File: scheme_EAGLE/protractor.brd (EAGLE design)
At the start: 160 x 100 mm, 20 parts, among them T1 BT136, U1 ATTINY45-20PU

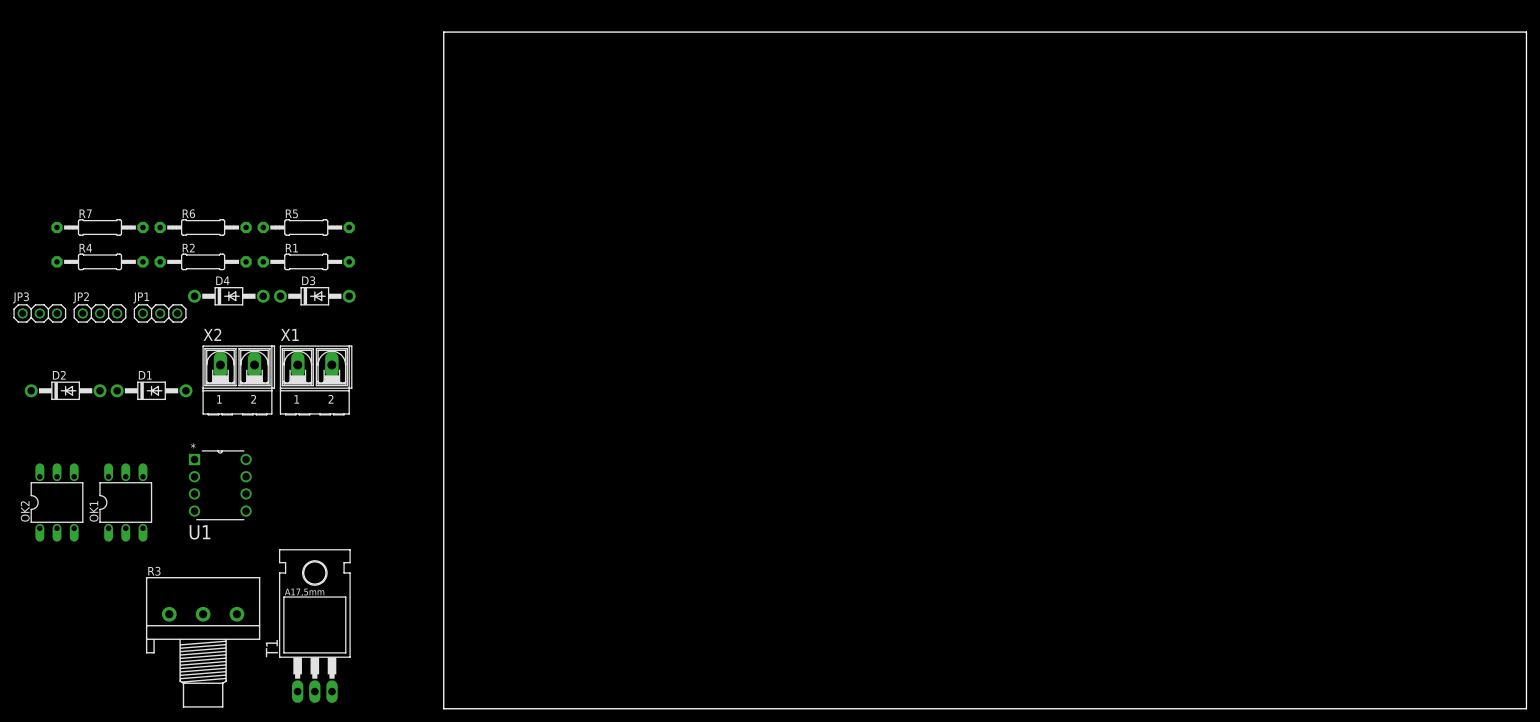
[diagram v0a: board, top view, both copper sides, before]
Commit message: Make the first version of the dimmer board
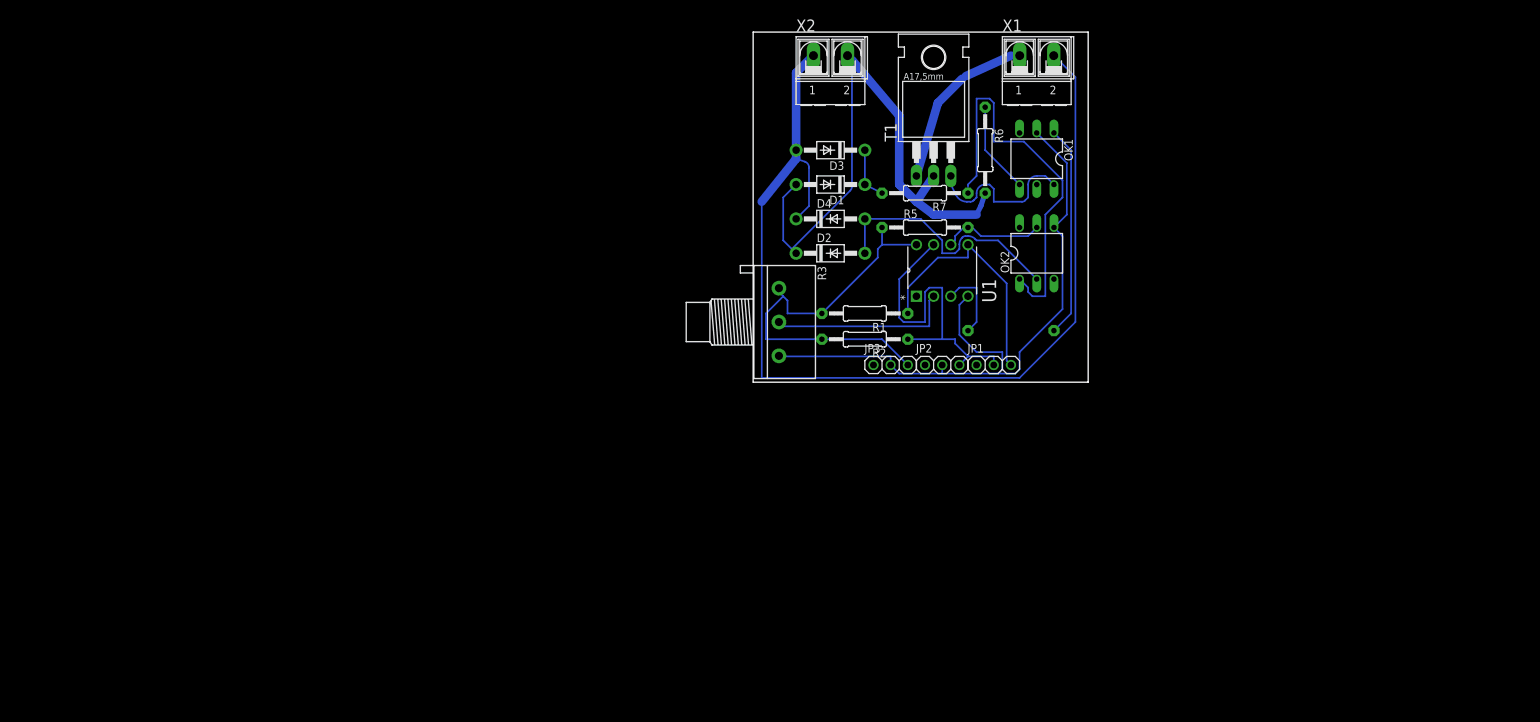
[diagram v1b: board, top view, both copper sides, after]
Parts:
- moved OK2 149.4 mm to (87.6, 67.3)
- moved OK1 143.9 mm to (87.6, 81.3), turned to 180 degrees
- moved R4 135.0 mm to (83.8, 55.9), flipped to the bottom, turned to 180 degrees
- moved JP3 126.0 mm to (66.0, 50.8)
- moved JP2 124.7 mm to (73.7, 50.8)
- moved JP1 123.4 mm to (81.3, 50.8)
- moved R7 122.0 mm to (71.1, 76.2), turned to 180 degrees
- moved T1 119.0 mm to (72.4, 85.1)
- moved R6 116.1 mm to (80.0, 82.5), turned to 270 degrees
- moved X1 116.1 mm to (87.6, 96.5)
- moved D2 114.8 mm to (57.1, 67.3)
- moved U1 113.7 mm to (77.5, 68.6), turned to 90 degrees
- moved D1 104.9 mm to (57.1, 77.5), turned to 180 degrees
- moved X2 98.8 mm to (57.1, 96.5)
- moved R2 98.5 mm to (62.2, 54.6), turned to 180 degrees
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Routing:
- net N$3: track 0.00 -> 151.8 mm
- net GND: track 0.00 -> 96.8 mm
- net N$4: track 0.00 -> 87.2 mm
- net VCC: track 0.00 -> 60.7 mm
- net N$5: track 0.00 -> 59.0 mm
- net N$14: track 0.00 -> 49.0 mm
- net N$1: track 0.00 -> 37.9 mm
- net N$11: track 0.00 -> 36.9 mm
- net N$13: track 0.00 -> 31.3 mm
- net N$9: track 0.00 -> 27.6 mm
- net N$8: track 0.00 -> 25.6 mm
- net N$6: track 0.00 -> 24.5 mm
- net N$10: track 0.00 -> 15.2 mm
- net N$7: track 0.00 -> 13.5 mm
- net N$12: track 0.00 -> 11.2 mm
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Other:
- board size 160 x 100 mm -> 49.5 x 51.7 mm

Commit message: Route configured.
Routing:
- net N$9: track 27.6 -> 58.7 mm
- net N$3: track 151.8 -> 179.0 mm
- net N$5: track 59.0 -> 37.4 mm
- net GND: track 96.8 -> 115.5 mm
- net N$14: track 49.0 -> 33.6 mm
- net N$1: track 37.9 -> 46.3 mm
- net N$6: track 24.5 -> 31.4 mm
- net N$4: track 87.2 -> 82.0 mm
- net N$12: track 11.2 -> 6.13 mm
- net N$8: track 25.6 -> 29.8 mm
- net N$11: track 36.9 -> 33.8 mm
- net N$13: track 31.3 -> 33.4 mm
- net VCC: track 60.7 -> 59.7 mm
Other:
- board size 49.5 x 51.7 mm -> 53.3 x 56.2 mm

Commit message: Now, the firmware is works
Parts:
- .: value ATTINY45-20PU -> attiny
- renumbered U1 to .
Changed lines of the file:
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@@
 <?xml version="1.0" encoding="utf-8"?>
 <!DOCTYPE eagle SYSTEM "eagle.dtd">
-<eagle version="7.2.0">
+<eagle version="7.5.0">
 <drawing>
 <settings>
@@
 <layer number="15" name="Route15" color="4" fill="6" visible="no" active="no"/>
 <layer number="16" name="Bottom" color="1" fill="1" visible="yes" active="yes"/>
-<layer number="17" name="Pads" color="2" fill="1" visible="yes" active="yes"/>
-<layer number="18" name="Vias" color="2" fill="1" visible="yes" active="yes"/>
-<layer number="19" name="Unrouted" color="6" fill="1" visible="yes" active="yes"/>
+<layer number="17" name="Pads" color="2" fill="1" visible="no" active="yes"/>
+<layer number="18" name="Vias" color="2" fill="1" visible="no" active="yes"/>
+<layer number="19" name="Unrouted" color="6" fill="1" visible="no" active="yes"/>
 <layer number="20" name="Dimension" color="15" fill="1" visible="yes" active="yes"/>
 <layer number="21" name="tPlace" color="7" fill="1" visible="yes" active="yes"/>
 <layer number="22" name="bPlace" color="7" fill="1" visible="yes" active="yes"/>
-<layer number="23" name="tOrigins" color="15" fill="1" visible="yes" active="yes"/>
-<layer number="24" name="bOrigins" color="15" fill="1" visible="yes" active="yes"/>
-<layer number="25" name="tNames" color="7" fill="1" visible="yes" active="yes"/>
-<layer number="26" name="bNames" color="7" fill="1" visible="yes" active="yes"/>
+<layer number="23" name="tOrigins" color="15" fill="1" visible="no" active="yes"/>
+<layer number="24" name="bOrigins" color="15" fill="1" visible="no" active="yes"/>
+<layer number="25" name="tNames" color="7" fill="1" visible="no" active="yes"/>
+<layer number="26" name="bNames" color="7" fill="1" visible="no" active="yes"/>
 <layer number="27" name="tValues" color="7" fill="1" visible="yes" active="yes"/>
 <layer number="28" name="bValues" color="7" fill="1" visible="yes" active="yes"/>
 <layer number="29" name="tStop" color="7" fill="3" visible="yes" active="yes"/>
-<layer number="30" name="bStop" color="7" fill="6" visible="yes" active="yes"/>
-<layer number="31" name="tCream" color="7" fill="4" visible="yes" active="yes"/>
-<layer number="32" name="bCream" color="7" fill="5" visible="yes" active="yes"/>
-<layer number="33" name="tFinish" color="6" fill="3" visible="yes" active="yes"/>
-<layer number="34" name="bFinish" color="6" fill="6" visible="yes" active="yes"/>
-<layer number="35" name="tGlue" color="7" fill="4" visible="yes" active="yes"/>
-<layer number="36" name="bGlue" color="7" fill="5" visible="yes" active="yes"/>
-<layer number="37" name="tTest" color="7" fill="1" visible="yes" active="yes"/>
-<layer number="38" name="bTest" color="7" fill="1" visible="yes" active="yes"/>
-<layer number="39" name="tKeepout" color="4" fill="11" visible="yes" active="yes"/>
-<layer number="40" name="bKeepout" color="1" fill="11" visible="yes" active="yes"/>
-<layer number="41" name="tRestrict" color="4" fill="10" visible="yes" active="yes"/>
-<layer number="42" name="bRestrict" color="1" fill="10" visible="yes" active="yes"/>
-<layer number="43" name="vRestrict" color="2" fill="10" visible="yes" active="yes"/>
-<layer number="44" name="Drills" color="7" fill="1" visible="yes" active="yes"/>
-<layer number="45" name="Holes" color="7" fill="1" visible="yes" active="yes"/>
-<layer number="46" name="Milling" color="3" fill="1" visible="yes" active="yes"/>
-<layer number="47" name="Measures" color="7" fill="1" visible="yes" active="yes"/>
-<layer number="48" name="Document" color="7" fill="1" visible="yes" active="yes"/>
-<layer number="49" name="Reference" color="7" fill="1" visible="yes" active="yes"/>
+<layer number="30" name="bStop" color="7" fill="6" visible="no" active="yes"/>
+<layer number="31" name="tCream" color="7" fill="4" visible="no" active="yes"/>
+<layer number="32" name="bCream" color="7" fill="5" visible="no" active="yes"/>
+<layer number="33" name="tFinish" color="6" fill="3" visible="no" active="yes"/>
+<layer number="34" name="bFinish" color="6" fill="6" visible="no" active="yes"/>
+<layer number="35" name="tGlue" color="7" fill="4" visible="no" active="yes"/>
+<layer number="36" name="bGlue" color="7" fill="5" visible="no" active="yes"/>
+<layer number="37" name="tTest" color="7" fill="1" visible="no" active="yes"/>
+<layer number="38" name="bTest" color="7" fill="1" visible="no" active="yes"/>
+<layer number="39" name="tKeepout" color="4" fill="11" visible="no" active="yes"/>
+<layer number="40" name="bKeepout" color="1" fill="11" visible="no" active="yes"/>
+<layer number="41" name="tRestrict" color="4" fill="10" visible="no" active="yes"/>
+<layer number="42" name="bRestrict" color="1" fill="10" visible="no" active="yes"/>
+<layer number="43" name="vRestrict" color="2" fill="10" visible="no" active="yes"/>
+<layer number="44" name="Drills" color="7" fill="1" visible="no" active="yes"/>
+<layer number="45" name="Holes" color="7" fill="1" visible="no" active="yes"/>
+<layer number="46" name="Milling" color="3" fill="1" visible="no" active="yes"/>
+<layer number="47" name="Measures" color="7" fill="1" visible="no" active="yes"/>
+<layer number="48" name="Document" color="7" fill="1" visible="no" active="yes"/>
+<layer number="49" name="Reference" color="7" fill="1" visible="no" active="yes"/>
 <layer number="50" name="dxf" color="7" fill="1" visible="no" active="no"/>
-<layer number="51" name="tDocu" color="7" fill="1" visible="yes" active="yes"/>
+<layer number="51" name="tDocu" color="7" fill="1" visible="no" active="yes"/>
 <layer number="52" name="bDocu" color="7" fill="1" visible="yes" active="yes"/>
 <layer number="53" name="tGND_GNDA" color="7" fill="9" visible="no" active="no"/>
@@
 <element name="R7" library="adafruit" package="0207/12" value="30k" x="71.12" y="76.2" rot="R180"/>
 <element name="T1" library="triac" package="TO220AB" value="BT136" x="72.39" y="85.09"/>
-<element name="U1" library="Atmel_By_element14_Batch_1-00" package="DIP254P762X533-8" value="ATTINY45-20PU" x="77.47" y="68.58" rot="R90">
+<element name="." library="Atmel_By_element14_Batch_1-00" package="DIP254P762X533-8" value="attiny" x="77.47" y="68.58" rot="R90">
 <attribute name="PACKAGE" value="PDIP-8" x="77.47" y="68.58" size="1.778" layer="27" rot="R90" display="off"/>
 <attribute name="OC_NEWARK" value="23M5072" x="77.47" y="68.58" size="1.778" layer="27" rot="R90" display="off"/>
@@
 <signal name="N$9">
 <contactref element="R3" pad="2"/>
-<contactref element="U1" pad="2"/>
+<contactref element="." pad="2"/>
 <wire x1="75.72375" y1="55.72125" x2="75.3042625" y2="55.72125" width="0.508" layer="16"/>
 <wire x1="75.3042625" y1="55.72125" x2="72.39" y2="58.6355125" width="0.508" layer="16" curve="-90"/>
@@
 <contactref element="R3" pad="3"/>
 <contactref element="JP3" pad="2"/>
-<contactref element="U1" pad="4"/>
+<contactref element="." pad="4"/>
 <contactref element="OK2" pad="4"/>
 <contactref element="OK1" pad="2"/>
@@
 <contactref element="R3" pad="1"/>
 <contactref element="JP3" pad="3"/>
-<contactref element="U1" pad="8"/>
+<contactref element="." pad="8"/>
 <contactref element="R5" pad="1"/>
 <contactref element="R1" pad="2"/>
@@
 <contactref element="R5" pad="2"/>
 <contactref element="OK2" pad="5"/>
-<contactref element="U1" pad="6"/>
+<contactref element="." pad="6"/>
 <wire x1="86.36" y1="69.85" x2="87.63" y2="71.12" width="0.508" layer="16"/>
 <wire x1="78.74" y1="69.85" x2="86.36" y2="69.85" width="0.508" layer="16"/>
@@
 </signal>
 <signal name="N$12">
-<contactref element="U1" pad="3"/>
+<contactref element="." pad="3"/>
 <contactref element="R4" pad="1"/>
 <wire x1="76.35875" y1="59.53125" x2="77.47" y2="58.42" width="0.508" layer="16" curve="-90"/>
@@
 <contactref element="JP1" pad="3"/>
 <contactref element="R1" pad="1"/>
-<contactref element="U1" pad="5"/>
+<contactref element="." pad="5"/>
 <wire x1="81.28" y1="53.34" x2="83.82" y2="50.8" width="0.508" layer="16"/>
 <wire x1="75.72375" y1="53.34" x2="81.28" y2="53.34" width="0.508" layer="16"/>
@@
 <contactref element="JP1" pad="2"/>
 <contactref element="R2" pad="1"/>
-<contactref element="U1" pad="7"/>
+<contactref element="." pad="7"/>
 <contactref element="JP2" pad="3"/>
 <wire x1="77.47" y1="52.07" x2="76.2" y2="50.8" width="0.508" layer="16"/>
